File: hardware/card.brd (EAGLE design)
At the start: 97 x 56 mm, 91 parts, among them J1 UE27AC54100, J2 MICROSD, J3 0541323062, J4 6-PIN_2MM-V, J5 JST_2PIN, J6 B2PS-VH(LF)(SN), J7 MINI-USB-UX60A-MB-5ST, J8 JST_2PIN, U1 ATSAMD21J_QFN, U2 TS3USB221, U3 MIC2288YD5-TR, U4 MCP73833, U5 TLV70233DBVR, X2 32.768, X3 ATWINC1500_MR210PA

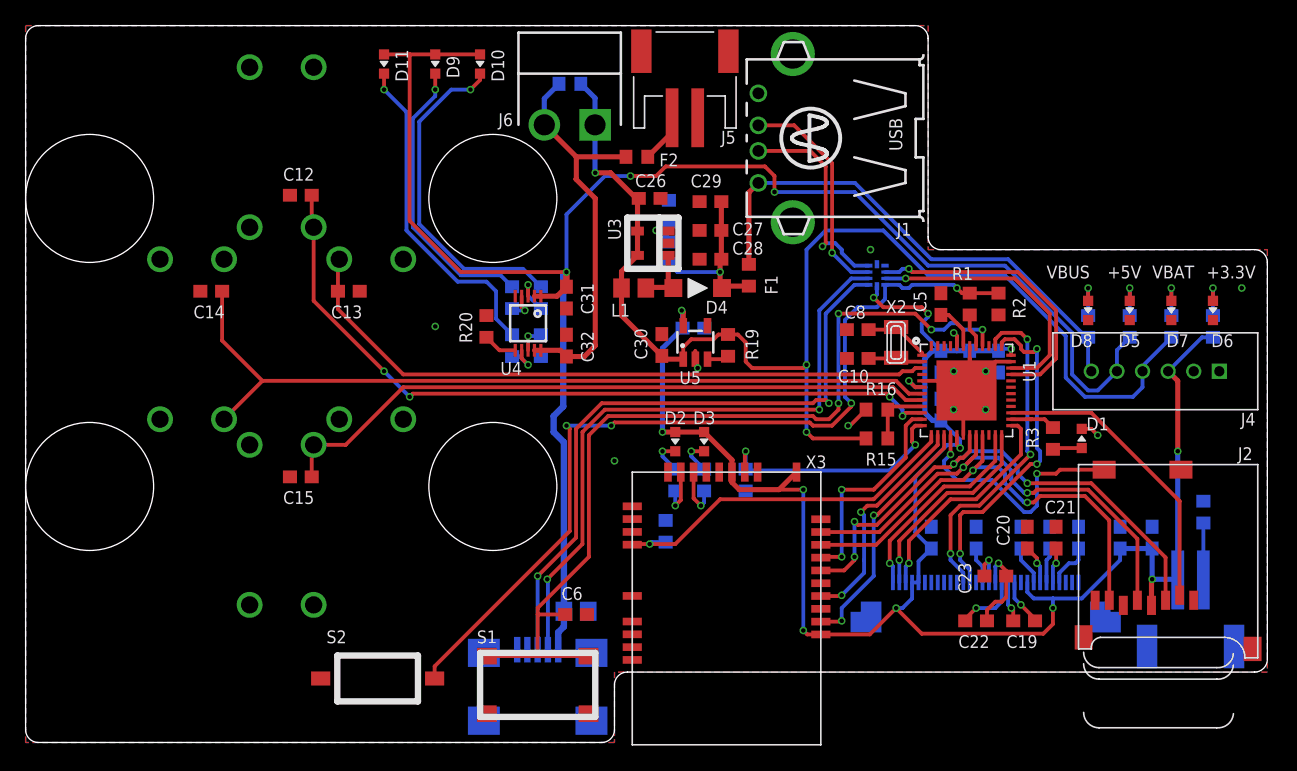
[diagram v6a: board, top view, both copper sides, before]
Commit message: silkscreen additions, fixed button labels
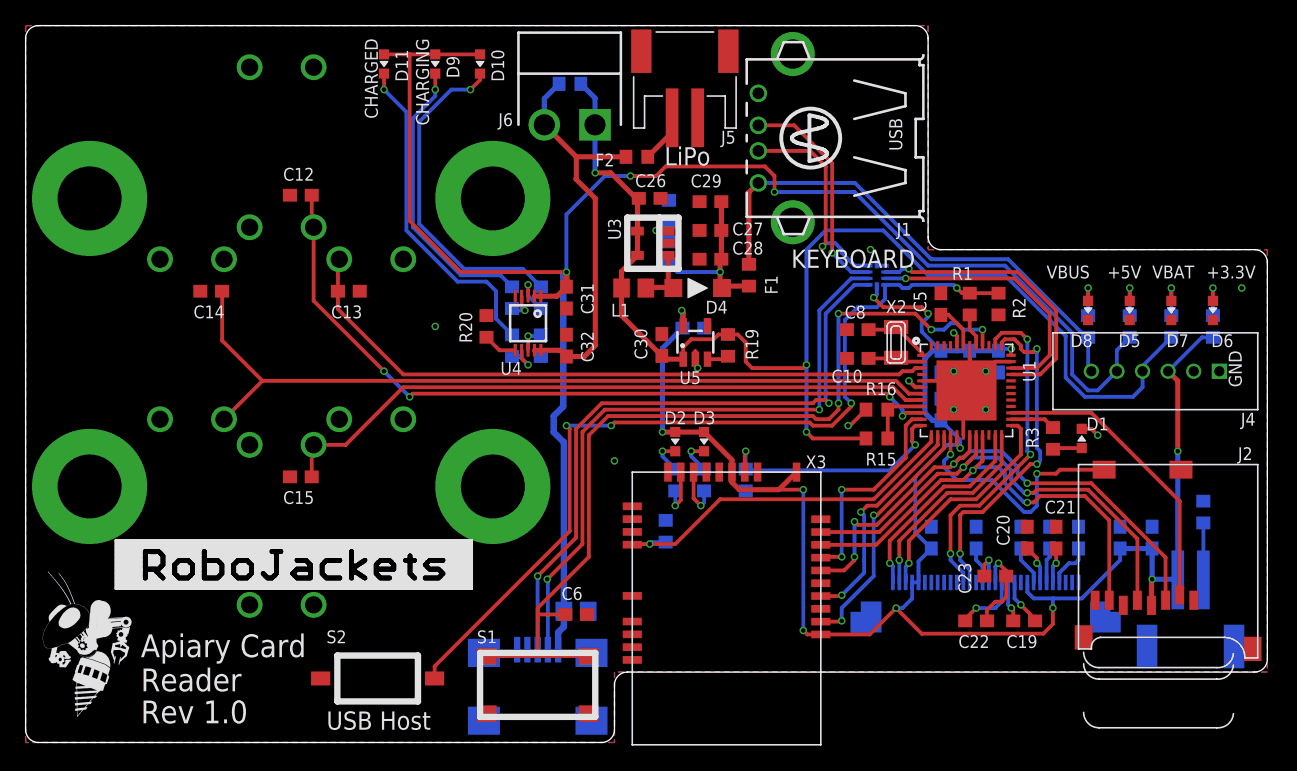
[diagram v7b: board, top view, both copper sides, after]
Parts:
- added U$1: (no value), RoboJackets-Aesthetics:ROBOBUZZ_0.6X
- added U$2: (no value), RoboJackets-Aesthetics:ROBOJACKETS
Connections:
- net BTN-DOWN: now also C15.1, S6.2, U1.8; no longer C13.1, S4.1, U1.3
- net BTN-LEFT: now also C13.1, S4.1, U1.3; no longer C14.1, S5.1, U1.7
- net BTN-RIGHT: now also C14.1, S5.1, U1.7; no longer C15.1, S6.2, U1.8
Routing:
- net BTN-LEFT: track 64.5 -> 51.9 mm
- net BTN-RIGHT: track 52.4 -> 64.5 mm
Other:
- board text added: "Apiary Card Reader"
- board text added: "CHARGED"
- board text added: "CHARGING"
- board text added: "GND"
- board text added: "KEYBOARD"
- board text added: "LCD"
- board text added: "LiPo"
- board text added: "Rev 1.0"
- board text added: "USB Host"
- board text added: "np"

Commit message: More tweaks, fix DRC error
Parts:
- moved R19 0.25 mm to (54.9, 31.3)
- moved U5 0.25 mm to (52.3, 31.5)
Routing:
- net GND: track 16.9 -> 15.8 mm
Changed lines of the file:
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@@
 <text x="42" y="51" size="1.016" layer="22" rot="MR180">np</text>
 <text x="60" y="11" size="1.4224" layer="22" font="vector" rot="MR180">LCD</text>
-<text x="96.5" y="15.5" size="1.4224" layer="22" font="vector" rot="MR0">LCD</text>
+<text x="95.75" y="15.5" size="1.4224" layer="22" font="vector" rot="MR0">LCD</text>
 <text x="30.5" y="55" size="1.016" layer="21" font="vector" rot="R270">CHARGING</text>
 <text x="26.5" y="55" size="1.016" layer="21" font="vector" rot="R270">CHARGED</text>
@@
 </class>
 </classes>
-<designrules name="eC_2Layer_PClass6_BaseCopperO18_eCDefault *">
+<designrules name="eC_2Layer_PClass6_BaseCopperO18_eCDefault">
 <description language="de">
 &lt;p&gt;
@@
 <param name="srMaxRoundness" value="0mil"/>
 <param name="slThermalIsolate" value="0.2mm"/>
-<param name="slThermalsForVias" value="0"/>
+<param name="slThermalsForVias" value="1"/>
 <param name="dpMaxLengthDifference" value="10mm"/>
 <param name="dpGapFactor" value="2.5"/>
@@
 </element>
 <element name="R4" library="rcl" library_urn="urn:adsk.eagle:library:334" package="R0603" package3d_urn="urn:adsk.eagle:package:23555/2" value="0" x="92" y="18" smashed="yes" rot="MR90">
-<attribute name="NAME" x="93.135" y="17.115" size="1" layer="26" rot="MR90"/>
+<attribute name="NAME" x="92.885" y="17.865" size="1" layer="26" rot="MR90"/>
 <attribute name="VALUE" x="90.095" y="17.365" size="1.27" layer="28" rot="MR90"/>
 </element>
@@
 <attribute name="VALUE" x="65.865" y="21.845" size="1.27" layer="27"/>
 </element>
-<element name="R19" library="rcl" library_urn="urn:adsk.eagle:library:334" package="R0603" package3d_urn="urn:adsk.eagle:package:23555/2" value="10k" x="54.87" y="31.02" smashed="yes" rot="R90">
-<attribute name="NAME" x="57.235" y="29.885" size="1" layer="25" rot="R90"/>
-<attribute name="VALUE" x="56.775" y="30.385" size="1.27" layer="27" rot="R90"/>
+<element name="R19" library="rcl" library_urn="urn:adsk.eagle:library:334" package="R0603" package3d_urn="urn:adsk.eagle:package:23555/2" value="10k" x="54.87" y="31.27" smashed="yes" rot="R90">
+<attribute name="NAME" x="57.235" y="30.135" size="1" layer="25" rot="R90"/>
+<attribute name="VALUE" x="56.775" y="30.635" size="1.27" layer="27" rot="R90"/>
 </element>
 <element name="R16" library="rcl" library_urn="urn:adsk.eagle:library:334" package="R0603" package3d_urn="urn:adsk.eagle:package:23555/2" value="10k 1%" x="66.5" y="26" smashed="yes" rot="R180">
@@
 <attribute name="VALUE" x="36.968" y="34.274" size="0.5" layer="27" ratio="10" rot="R270"/>
 </element>
-<element name="U5" library="lib-card" package="SOT-23-5" value="TLV70233DBVR" x="52.32" y="31.25" smashed="yes">
-<attribute name="DIGIKEY" value="296-32415-1-ND" x="52.32" y="31.25" size="1.778" layer="27" display="off"/>
-<attribute name="MPN" value="TLV70233DBVR" x="52.32" y="31.25" size="1.778" layer="27" display="off"/>
-<attribute name="NAME" x="51.07" y="28" size="1" layer="25" ratio="10"/>
+<element name="U5" library="lib-card" package="SOT-23-5" value="TLV70233DBVR" x="52.32" y="31.5" smashed="yes">
+<attribute name="DIGIKEY" value="296-32415-1-ND" x="52.32" y="31.5" size="1.778" layer="27" display="off"/>
+<attribute name="MPN" value="TLV70233DBVR" x="52.32" y="31.5" size="1.778" layer="27" display="off"/>
+<attribute name="NAME" x="51.07" y="28.25" size="1" layer="25" ratio="10"/>
 </element>
 <element name="X3" library="CardReader" package="ATWINC1500_MR210PA" value="ATWINC1500_MR210PA" x="54.5" y="13.5" smashed="yes" rot="R180">
@@
 <wire x1="76.975" y1="29.75" x2="75.75" y2="29.75" width="0.3" layer="1"/>
 <wire x1="75.75" y1="29.75" x2="75.5" y2="29.5" width="0.3" layer="1"/>
-<wire x1="73.75" y1="30.975" x2="73.75" y2="30" width="0.3" layer="1"/>
-<wire x1="73.75" y1="30" x2="73.75" y2="29.75" width="0.3" layer="1"/>
+<wire x1="73.75" y1="30.975" x2="73.75" y2="29.75" width="0.3" layer="1"/>
 <wire x1="73.5" y1="29.5" x2="73.75" y2="29.75" width="0.3" layer="1"/>
 <polygon width="0.3" layer="16">
@@
 <wire x1="73.5" y1="27.5" x2="73.5" y2="26" width="0.3" layer="1"/>
 <wire x1="73.5" y1="26" x2="72.5" y2="26" width="0.3" layer="1"/>
-<wire x1="73.75" y1="30" x2="73.75" y2="27.5" width="0.3" layer="1"/>
+<wire x1="73.75" y1="29.75" x2="73.75" y2="27.5" width="0.3" layer="1"/>
 <wire x1="73.75" y1="27.5" x2="73.5" y2="27.5" width="0.3" layer="1"/>
-<wire x1="52.32" y1="29.944" x2="52.32" y2="30.57" width="0.3" layer="1"/>
-<wire x1="52.32" y1="30.57" x2="52.5" y2="29.25" width="0.3" layer="1"/>
-<via x="52.5" y="29.25" extent="1-16" drill="0.35"/>
+<wire x1="52.32" y1="30.57" x2="52.32" y2="30.194" width="0.3" layer="1"/>
+<via x="52.5" y="29.5" extent="1-16" drill="0.35"/>
 <wire x1="65.65" y1="26" x2="64.4" y2="24.75" width="0.3" layer="1"/>
 <wire x1="64.4" y1="24.75" x2="64.25" y2="24.75" width="0.3" layer="1"/>
@@
 <contactref element="S4" pad="4"/>
 <contactref element="S3" pad="4"/>
+<wire x1="52.32" y1="30.194" x2="52.32" y2="29.68" width="0.3" layer="1"/>
+<wire x1="52.32" y1="29.68" x2="52.5" y2="29.5" width="0.3" layer="1"/>
 </signal>
 <signal name="D-">
@@
 <via x="51.25" y="33.75" extent="1-16" drill="0.35"/>
 <wire x1="51.25" y1="33.75" x2="51.37" y2="33.63" width="0.4" layer="1"/>
-<wire x1="51.37" y1="33.63" x2="51.37" y2="32.556" width="0.4" layer="1"/>
+<wire x1="51.37" y1="33.63" x2="51.37" y2="32.806" width="0.4" layer="1"/>
 <wire x1="71.5" y1="30.6" x2="70" y2="32.1" width="0.3" layer="16"/>
 <wire x1="70" y1="32.1" x2="70" y2="32.75" width="0.3" layer="16"/>
@@
 <wire x1="46.55" y1="33.35" x2="49.7" y2="30.2" width="0.4" layer="1"/>
 <wire x1="46.55" y1="33.35" x2="46.55" y2="35.5" width="0.4" layer="1"/>
-<wire x1="49.7" y1="30.2" x2="49.956" y2="29.944" width="0.4" layer="1"/>
-<wire x1="49.956" y1="29.944" x2="51.37" y2="29.944" width="0.4" layer="1"/>
+<wire x1="49.7" y1="30.2" x2="49.956" y2="30.194" width="0.4" layer="1"/>
+<wire x1="49.956" y1="30.194" x2="51.37" y2="30.194" width="0.4" layer="1"/>
 <wire x1="65.65" y1="23.75" x2="61.5" y2="23.75" width="0.3" layer="1"/>
 <wire x1="61.5" y1="23.75" x2="61" y2="24.25" width="0.3" layer="1"/>
@@
 <wire x1="56.75" y1="29.25" x2="56.25" y2="29.75" width="0.3" layer="1"/>
 <wire x1="56.25" y1="29.75" x2="56.25" y2="31.25" width="0.3" layer="1"/>
-<wire x1="56.25" y1="31.25" x2="55.63" y2="31.87" width="0.3" layer="1"/>
-<wire x1="55.63" y1="31.87" x2="54.87" y2="31.87" width="0.3" layer="1"/>
-<wire x1="54.87" y1="31.87" x2="54.12" y2="31.87" width="0.3" layer="1"/>
-<wire x1="54.12" y1="31.87" x2="53.75" y2="31.5" width="0.3" layer="1"/>
+<wire x1="56.25" y1="31.25" x2="55.38" y2="32.12" width="0.3" layer="1"/>
+<wire x1="55.38" y1="32.12" x2="54.87" y2="32.12" width="0.3" layer="1"/>
+<wire x1="54.87" y1="32.12" x2="54.37" y2="32.12" width="0.3" layer="1"/>
+<wire x1="54.37" y1="32.12" x2="53.75" y2="31.5" width="0.3" layer="1"/>
 <wire x1="52" y1="31.5" x2="53.75" y2="31.5" width="0.3" layer="1"/>
-<wire x1="51.37" y1="29.944" x2="51.37" y2="30.87" width="0.3" layer="1"/>
+<wire x1="51.37" y1="30.194" x2="51.37" y2="30.87" width="0.3" layer="1"/>
 <wire x1="51.37" y1="30.87" x2="52" y2="31.5" width="0.3" layer="1"/>
 <wire x1="61" y1="29.5" x2="61" y2="38.5" width="0.3" layer="16"/>
@@
 <contactref element="U5" pad="3"/>
 <contactref element="R19" pad="1"/>
-<wire x1="53.27" y1="29.944" x2="54.644" y2="29.944" width="0.3" layer="1"/>
-<wire x1="54.644" y1="29.944" x2="54.87" y2="30.17" width="0.3" layer="1"/>
+<wire x1="53.27" y1="30.194" x2="54.644" y2="30.194" width="0.3" layer="1"/>
+<wire x1="54.644" y1="30.194" x2="54.87" y2="30.42" width="0.3" layer="1"/>
 </signal>
 <signal name="BATT">
@@
 </signal>
 <signal name="N$1">
-<via x="36.5" y="42.5" extent="1-16" drill="5" diameter="9"/>
+<via x="36.5" y="42.5" extent="1-16" drill="5.5" diameter="9"/>
 </signal>
 <signal name="N$2">
-<via x="5" y="42.5" extent="1-16" drill="5" diameter="9"/>
+<via x="5" y="42.5" extent="1-16" drill="5.5" diameter="9"/>
 </signal>
 <signal name="N$3">
-<via x="5" y="20" extent="1-16" drill="5" diameter="9"/>
+<via x="5" y="20" extent="1-16" drill="5.5" diameter="9"/>
 </signal>
 <signal name="N$4">
-<via x="36.5" y="20" extent="1-16" drill="5" diameter="9"/>
+<via x="36.5" y="20" extent="1-16" drill="5.5" diameter="9"/>
 </signal>
 </signals>
